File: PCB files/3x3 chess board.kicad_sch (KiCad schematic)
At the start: 81 parts, among them J1 Conn_01x03, J10 Conn_01x02, J11 USB4216-03-A_REVA, J12 Conn_01x03, J2 Conn_01x03, J4 Conn_01x03, J5 Conn_01x03, J6 Conn_01x03, J7 Conn_01x03, J8 Conn_01x03, J9 Conn_01x03, U1 MCP23S17_SO, U2 MCP23S17_SO, U3 W25Q128JVS, U4 RP2040, X1 ABM8-272-T3

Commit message: update
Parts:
- added D10: LED, symbol Device:LED
- added R25, R26, R27, R28: R, symbol Device:R
- added SW1, SW2: SW_DPST_x2, symbol Switch:SW_DPST_x2
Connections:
- net +3.3V: now also R25.1, R27.1, R28.1; no longer D1.2 (A), D2.2 (A), D3.2 (A), D4.2 (A), D5.2 (A), D6.2 (A), D7.2 (A), D8.2 (A), D9.2 (A), U1.18 (~{RESET}), U2.18 (~{RESET})
- net GND: now also D1.1 (K), D2.1 (K), D3.1 (K), D4.1 (K), D5.1 (K), D6.1 (K), D7.1 (K), D8.1 (K), D9.1 (K), D10.1 (K), SW1.1 (A), SW2.1 (A)
- net at R7.2: now also D5.2 (A); no longer D7.1 (K)
- net at R5.2: now also D7.2 (A); no longer D5.1 (K)
- net at R1.2: now also D2.2 (A); no longer D4.1 (K)
- net at R3.1: now also D4.2 (A); no longer D2.1 (K)
- net at R4.2: now also D3.2 (A); no longer D3.1 (K)
- net at R9.2: now also D9.2 (A); no longer D9.1 (K)
- net at R8.2: now also D8.2 (A); no longer D8.1 (K)
- net at R6.2: now also D6.2 (A); no longer D6.1 (K)
- net at R2.2: now also D1.2 (A); no longer D1.1 (K)
- new net: R28.2, SW1.2 (B), U1.18 (~{RESET})
- new net: R27.2, SW2.2 (B), U2.18 (~{RESET})
- new net: D10.2 (A), R25.2
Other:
- note added: "replace with esp 32 and esp prog"
- note added: "testing voltage regulator"
- moved on the sheet: D1, D2, D3, D4, D5, D6, D7, D8, D9, TP1, TP2, TP3

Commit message: update
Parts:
- removed C2: 0.1uF, Capacitor_SMD:C_0805_2012Metric, symbol Device:C
- removed C21, C22: 1uF, Capacitor_SMD:C_0805_2012Metric_Pad1.18x1.45mm_HandSolder, symbol Device:C
- removed J10: Conn_01x02, Connector_PinHeader_2.54mm:PinHeader_1x02_P2.54mm_Vertical, symbol Connector_Generic:Conn_01x02
- removed J11: USB4216-03-A_REVA, USB receptacle:USB 2.0, symbol USB C 2.0 receptacle:USB4216-03-A_REVA
- removed R27: R, symbol Device:R
- removed SW2: SW_DPST_x2, symbol Switch:SW_DPST_x2
- removed TP10, TP4, TP5, TP7, TP8: TestPoint, TestPoint:TestPoint_Pad_2.0x2.0mm, symbol Connector:TestPoint
- removed U2: MCP23S17_SO, Package_SO:SOIC-28W_7.5x17.9mm_P1.27mm, symbol Interface_Expansion:MCP23S17_SO
- removed U3: W25Q128JVS, Package_SO:SOIC-8_5.3x5.3mm_P1.27mm, symbol Memory_Flash:W25Q128JVS
- removed U4: RP2040, Package_DFN_QFN:QFN-56-1EP_7x7mm_P0.4mm_EP3.2x3.2mm, symbol MCU_RaspberryPi:RP2040
- removed X1: ABM8-272-T3, ABM8 - 272 - T3:ABM8-272-T3_ABR, symbol ABM8-272-T3:ABM8-272-T3
- added D11: LED, symbol Device:LED
- added D12, D13, D14, D15, D16, D17, D18: LED, Diode_SMD:D_0805_2012Metric_Pad1.15x1.40mm_HandSolder, symbol Device:LED
- added J10, J11, J13, J14, J15, J16, J17: Conn_01x03, Hall effect sensor:TSOT-3L_MLX92232LSE-AAA-002-SP_MEL, symbol Connector_Generic:Conn_01x03
- added J3: Conn_02x03_Odd_Even, symbol Connector_Generic:Conn_02x03_Odd_Even
- added R29: 5k, Resistor_SMD:R_0805_2012Metric_Pad1.20x1.40mm_HandSolder, symbol Device:R
- added R30: R, symbol Device:R
- added R31, R32, R33, R34, R35, R36, R37: 16, Resistor_SMD:R_0805_2012Metric_Pad1.20x1.40mm_HandSolder, symbol Device:R
- added U3: ESP32-S3-WROOM-1, RF_Module:ESP32-S3-WROOM-1, symbol RF_Module:ESP32-S3-WROOM-1
- C14, C15: value 15pF -> 10nF
- C16, C17, C18, C19, C20: value 0.1uF -> 10nF
- R10: value 1k -> R; footprint Resistor_SMD:R_0805_2012Metric_Pad1.20x1.40mm_HandSolder -> (none)
- R11: value do not fit -> R; footprint Resistor_SMD:R_0805_2012Metric_Pad1.20x1.40mm_HandSolder -> (none)
- R12: value 1k -> 5k
- R13, R14: value 27.4 -> 5k; footprint Resistor_SMD:R_1210_3225Metric_Pad1.30x2.65mm_HandSolder -> Resistor_SMD:R_0805_2012Metric_Pad1.20x1.40mm_HandSolder
- R15, R16: value 5.1kΩ -> 5k
- R26: value R -> 5k; footprint (none) -> Resistor_SMD:R_0805_2012Metric_Pad1.20x1.40mm_HandSolder
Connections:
- net +1V1 is gone; now on net GND: C17.1
- net D+ is gone; now on net HALL11: R13.1
- net D- is gone; now on net HALL12: R14.1
- net XIN is gone; now on net +3.3V: C14.2
- net XOUT is gone; now on net +3.3V: R12.2
- net +3.3V: now also C15.2, C16.2, C17.2, C18.2, C19.2, C20.2, R11.2, R13.2, R14.2, R15.2, R16.2, R26.2, J10.1 (Pin_1), J11.1 (Pin_1), J13.1 (Pin_1), J14.1 (Pin_1), J15.1 (Pin_1), J16.1 (Pin_1), J17.1 (Pin_1), J3.2 (Pin_2), R29.2, U3.2 (3V3); no longer C16.1, C18.1, C19.1, C20.1, R11.1
- net CS_{extender1}: now also U3.10 (IO17)
- net CS_{extender2}: now also U3.11 (IO18)
- net GND: now also C15.1, C16.1, C18.1, C19.1, C20.1, D11.1 (K), D12.1 (K), D13.1 (K), D14.1 (K), D15.1 (K), D16.1 (K), D17.1 (K), D18.1 (K), J10.2 (Pin_2), J11.2 (Pin_2), J13.2 (Pin_2), J14.2 (Pin_2), J15.2 (Pin_2), J16.2 (Pin_2), J17.2 (Pin_2), J3.4 (Pin_4), U3.1 (GND), U3.40 (GND), U3.41 (GND); no longer C15.2, C16.2, C17.2, C18.2, C19.2, C20.2, R15.2, R16.2
- net HALL1: now also U1.1 (GPB0), R34.2; no longer U1.25 (GPA4)
- net HALL2: now also U1.2 (GPB1), R33.2; no longer U1.27 (GPA6)
- net HALL3: now also R5.2, U1.3 (GPB2); no longer U1.22 (GPA1)
- net HALL4: now also R3.2, U1.4 (GPB3)
- net HALL5: now also U1.5 (GPB4), R35.2
- net HALL6: now also U1.6 (GPB5), R32.2
- net HALL7: now also R6.2, U1.7 (GPB6)
- net HALL8: now also R1.2, U1.8 (GPB7)
- net HALL9: now also U1.21 (GPA0), R36.2
- net INTA_{extender1}: now also U3.39 (IO1)
- net INTA_{extender2}: now also U3.15 (IO3)
- net INTB_{extender1}: now also U3.38 (IO2)
- net INTB_{extender2}: now also U3.4 (IO4)
- net MISO: now also U3.21 (IO13)
- net MOSI: now also U3.19 (IO11)
- net SCK: now also U3.20 (IO12)
- net at R7.1: now also D7.2 (A); no longer U1.26 (GPA5)
- net at D5.2 (A): now also R5.1; no longer R7.2
- net HALL14: now reaches R16.1
- net HALL14: now also R9.2, U1.26 (GPA5), J15.3 (Pin_3)
- net HALL10: now reaches R12.1
- net HALL10: now also U1.22 (GPA1), J10.3 (Pin_3), R31.2; no longer C15.1
- net at D3.2 (A): now also R4.1; no longer R4.2
- net HALL13: now reaches R15.1
- net HALL13: now also U1.25 (GPA4), J14.3 (Pin_3), R37.2
- net HALL11: now reaches U1.23 (GPA2)
- net HALL11: now also R7.2, J11.3 (Pin_3); no longer R5.1
- net at R6.1: now also D6.2 (A); no longer U1.24 (GPA3)
- net at R1.1: now also D1.2 (A); no longer U1.28 (GPA7)
- net at D2.2 (A): now also R2.1; no longer R1.2
- net at D9.2 (A): now also R9.1; no longer R9.2
- net at D8.2 (A): now also R8.1; no longer R8.2
- net HALL15: now reaches R26.1
- net HALL15: now also R8.2, U1.27 (GPA6), J16.3 (Pin_3)
- net HALL12: now reaches R2.2
- net HALL12: now also U1.24 (GPA3), J13.3 (Pin_3); no longer D1.2 (A)
- net CS_{flash}: no longer names the net of R10.2
- net CS_{flash}: no longer R11.2
- new net: D14.2 (A), R33.1
- new net: D18.2 (A), R37.1
- new net: D13.2 (A), R32.1
- new net: D12.2 (A), R31.1
- new net: D11.2 (A), R30.2
- new net: D15.2 (A), R34.1
- new net: D16.2 (A), R35.1
- new net: D17.2 (A), R36.1
- new net EN: J3.1 (Pin_1), R11.1, U3.3 (EN)
- new net HALL16: J17.3 (Pin_3), R29.1, R4.2, U1.28 (GPA7)
- new net IO0: J3.6 (Pin_6), U3.27 (IO0)
- new net LED_test: R30.1, U3.23 (IO21)
- new net RX: J3.5 (Pin_5), U3.36 (RXD0)
- new net TX: J3.3 (Pin_3), U3.37 (TXD0)
- no-connect marks 35 -> 5
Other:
- note added: "Hall effect sensor 10"
- note added: "Hall effect sensor 11"
- note added: "Hall effect sensor 12"
- note added: "Hall effect sensor 13"
- note added: "Hall effect sensor 14"
- note added: "Hall effect sensor 15"
- note added: "Hall effect sensor 16"
- note added: "testing MCU"
- note removed: "MLX92213"
- note removed: "RP2040 MCU"
- note removed: "connect pin 1 and 2 w/ jumper to pull CS low"
- note removed: "replace with esp 32 and esp prog"
- note removed: "we can technically have 8 extenders per one cs, but i think we just use mult cs"
- moved on the sheet: C1, C10, C11, C12, C13, C3, C4, C5, C6, C7, C8, C9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

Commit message: update schematic and and pcb w/ new mcu
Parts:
- removed C8: 10uF, Capacitor_SMD:C_0805_2012Metric, symbol Device:C
- removed D17, D18: LED, Diode_SMD:D_0805_2012Metric_Pad1.15x1.40mm_HandSolder, symbol Device:LED
- removed LMS1585: ~, LMS1585:KTT0003B, symbol LM5158:LMS1585
- removed R1, R31, R32, R33, R34, R35, R36, R37, R6: 16, Resistor_SMD:R_0805_2012Metric_Pad1.20x1.40mm_HandSolder, symbol Device:R
- removed R25: R, symbol Device:R
- removed SW1: SW_DPST_x2, symbol Switch:SW_DPST_x2
- removed TP1, TP3, TP6: TestPoint, TestPoint:TestPoint_Pad_2.0x2.0mm, symbol Connector:TestPoint
- removed TP2: Ground test point, TestPoint:TestPoint_Pad_2.0x2.0mm, symbol Connector:TestPoint
- added C2, C22: 0.1uF, Capacitor_SMD:C_0805_2012Metric, symbol Device:C
- added C21, C4: 1uF, Capacitor_SMD:C_0805_2012Metric, symbol Device:C
- added D11: LED, Diode_SMD:D_0805_2012Metric_Pad1.15x1.40mm_HandSolder, symbol Device:LED
- added R11, R12, R13, R14, R15, R16, R17, R18, R3: 16, Resistor_SMD:R_0805_2012Metric_Pad1.20x1.40mm_HandSolder, symbol Device:R
- added U2: MCP23S17_SO, Package_SO:SOIC-28W_7.5x17.9mm_P1.27mm, symbol Interface_Expansion:MCP23S17_SO
- C3: value 10uF -> 1uF
- D10: footprint (none) -> Diode_SMD:D_0805_2012Metric_Pad1.15x1.40mm_HandSolder
- D17: renamed from D11; footprint (none) -> Diode_SMD:D_0805_2012Metric_Pad1.15x1.40mm_HandSolder
- J17: renamed from J3; footprint (none) -> Connector_IDC:IDC-Header_2x03_P2.54mm_Vertical
- R1: renamed from R28; value R -> 5k; footprint (none) -> Resistor_SMD:R_0805_2012Metric_Pad1.20x1.40mm_HandSolder
- R10: value R -> 16; footprint (none) -> Resistor_SMD:R_0805_2012Metric_Pad1.20x1.40mm_HandSolder
- R2: value 16 -> 5k
- R30: value R -> 320; footprint (none) -> Resistor_SMD:R_0805_2012Metric_Pad1.20x1.40mm_HandSolder
- R35: renamed from R11; value R -> 5k; footprint (none) -> Resistor_SMD:R_0805_2012Metric_Pad1.20x1.40mm_HandSolder
- renumbered C5 to C10, C4 to C11, C13 to C12, C15 to C13, C16 to C14, C14 to C15, C7 to C16, C19 to C17, C20 to C18, C17 to C19, C18 to C20, C12 to C5, C9 to C6, C10 to C7, C11 to C8, C6 to C9, J5 to J1, J13 to J10, J10 to J11, J2 to J12, J16 to J13, J17 to J14, J14 to J15, J15 to J16, J7 to J2, J6 to J3, J12 to J4, J9 to J5, J1 to J6, J4 to J7, J11 to J9, R18 to R19, R22 to R20, R17 to R21, R19 to R22, R20 to R23, R21 to R24, R23 to R25, R13 to R26, R14 to R27, R12 to R28, R24 to R29, R26 to R31, R29 to R32, R15 to R33, R16 to R34, R3 to R6
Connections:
- net VBUS is gone; now on net GND: C3.1
- net +3.3V: now also C3.2, R2.1, C2.2, C21.2, C22.2, C4.2, U2.9 (VDD)
- net CS_{extender1}: now also U3.24 (IO47); no longer U1.11 (~{CS}), U3.10 (IO17)
- net CS_{extender2}: now also U3.25 (IO48), U2.11 (~{CS}); no longer U3.11 (IO18)
- net GND: now also C2.1, C21.1, C22.1, C4.1, D11.1 (K), U2.10 (VSS), U2.15 (A0), U2.16 (A1), U2.17 (A2); no longer C3.2
- net HALL10: now also U2.2 (GPB1); no longer U1.22 (GPA1)
- net HALL11: now also U2.3 (GPB2); no longer R7.2, U1.23 (GPA2)
- net HALL12: now also U2.4 (GPB3); no longer R2.2, U1.24 (GPA3)
- net HALL13: now also U2.5 (GPB4); no longer U1.25 (GPA4)
- net HALL14: now also U2.6 (GPB5); no longer R9.2, U1.26 (GPA5)
- net HALL15: now also U2.7 (GPB6); no longer R8.2, U1.27 (GPA6)
- net HALL16: now also U2.8 (GPB7); no longer R4.2, U1.28 (GPA7)
- net HALL3: no longer R5.2
- net HALL4: no longer R6.2
- net HALL9: now also U2.1 (GPB0); no longer U1.21 (GPA0)
- net INTA_{extender1}: now also U3.17 (IO9); no longer U3.39 (IO1)
- net INTA_{extender2}: now also U2.20 (INTA)
- net INTB_{extender1}: now also U3.18 (IO10); no longer U3.38 (IO2)
- net INTB_{extender2}: now also U3.16 (IO46), U2.19 (INTB); no longer U3.4 (IO4)
- net LED_test: now also U3.5 (IO5); no longer U3.23 (IO21)
- net MISO: now also U2.14 (SO)
- net MOSI: now also U2.13 (SI)
- net SCK: now also U2.12 (SCK)
- net at D14.2 (A): now also R16.2
- net at D3.2 (A): now also R5.2; no longer R4.1
- net at D6.2 (A): now also R8.2
- net at D2.2 (A): now also R4.2; no longer R2.1
- net at R7.1: now also U1.25 (GPA4); no longer D7.2 (A)
- net at R8.1: now also U1.26 (GPA5); no longer D8.2 (A)
- net at D13.2 (A): now also R15.2
- net at D12.2 (A): now also R14.2
- net at D15.2 (A): now also R17.2
- net at D1.2 (A): now also R3.2
- net at D16.2 (A): now also R18.2
- net at R9.1: now also U1.27 (GPA6); no longer D9.2 (A)
- net at R10.1: now also U1.28 (GPA7)
- net at R10.2: now also D8.2 (A)
- net at D10.2 (A): now also R12.2
- net at D5.2 (A): now also R7.2; no longer R5.1
- new net: R17.1, U2.27 (GPA6)
- new net: R6.2, U1.24 (GPA3)
- new net: D11.2 (A), R13.2
- new net: D7.2 (A), R9.2
- new net: R3.1, U1.21 (GPA0)
- new net: R4.1, U1.22 (GPA1)
- new net: R5.1, U1.23 (GPA2)
- new net: R16.1, U2.26 (GPA5)
- new net: R2.2, U2.18 (~{RESET})
- new net: D9.2 (A), R11.2
- new net: R15.1, U2.25 (GPA4)
- new net: R12.1, U2.22 (GPA1)
- new net: R13.1, U2.23 (GPA2)
- new net: R14.1, U2.24 (GPA3)
- new net: R18.1, U2.28 (GPA7)
- new net: R11.1, U2.21 (GPA0)
- no-connect marks 5 -> 23
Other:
- note added: "esp PROG"
- note removed: "3.3 voltage regulator"
- note removed: "active low resets internally"
- note removed: "testing voltage regulator"
- moved on the sheet: C1, C10, C11, C12, C13, C14, C15, C16, C17, C18, C19, C20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

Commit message: changes
added promotion buttons, removed interrupts, cleaned up silkscreen
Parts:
- added R36: 5k, Resistor_SMD:R_0805_2012Metric_Pad1.20x1.40mm_HandSolder, symbol Device:R
- added R37, R38, R39, R40: 10k, Resistor_SMD:R_0805_2012Metric_Pad1.20x1.40mm_HandSolder, symbol Device:R
- added SW1, SW2, SW3, SW4: SW_Push, Button_Switch_THT:SW_PUSH_6mm_H4.3mm, symbol Switch:SW_Push
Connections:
- net +3.3V: now also R36.2, R37.2, R38.2, R39.2, R40.2
- net IO0: now also R36.1
- net Bishop_promote: now reaches U3.10 (IO17)
- net Bishop_promote: now also SW1.1
- net Rook_promote: now reaches U3.11 (IO18)
- net Rook_promote: now also SW2.1
- net Queen_promote: now reaches U3.12 (IO8)
- net Queen_promote: now also SW4.1
- net Knight_promote: now reaches U3.9 (IO16)
- net Knight_promote: now also SW3.1
- net INTA_{extender1}: no longer names the net of U3.17 (IO9)
- net INTA_{extender1}: no longer U1.20 (INTA)
- net INTA_{extender2}: no longer names the net of U3.15 (IO3)
- net INTA_{extender2}: no longer U2.20 (INTA)
- net INTB_{extender1}: no longer names the net of U3.18 (IO10)
- net INTB_{extender1}: no longer U1.19 (INTB)
- net INTB_{extender2}: no longer names the net of U3.16 (IO46)
- net INTB_{extender2}: no longer U2.19 (INTB)
- new net: R40.1, SW3.2
- new net: R39.1, SW1.2
- new net: R38.1, SW4.2
- new net: R37.1, SW2.2
- no-connect marks 23 -> 27
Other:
- moved on the sheet: C21, C22, J17, R35, U3

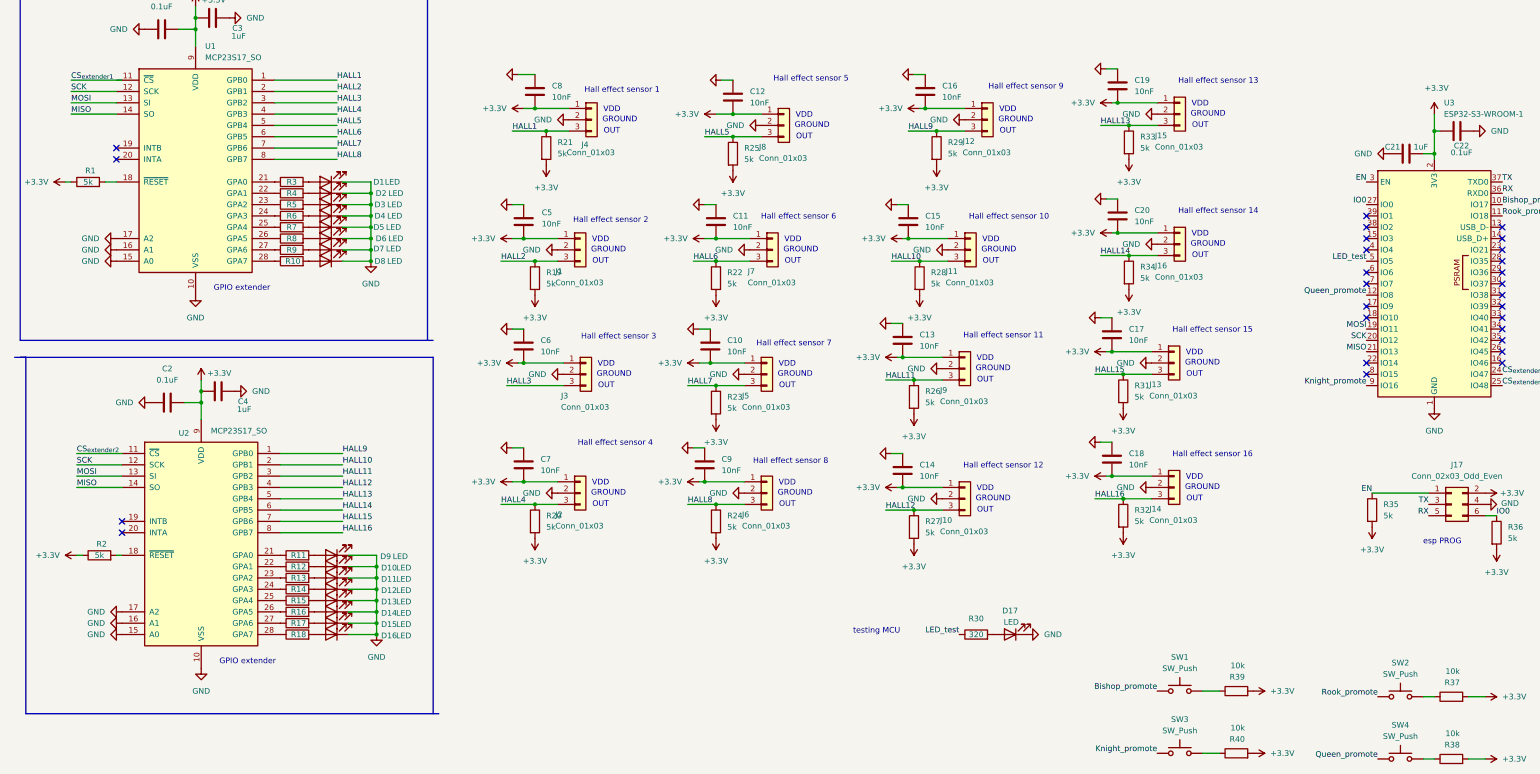
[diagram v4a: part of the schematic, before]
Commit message: adjustments before ordering
udpated res values, added gerber files and parts list files
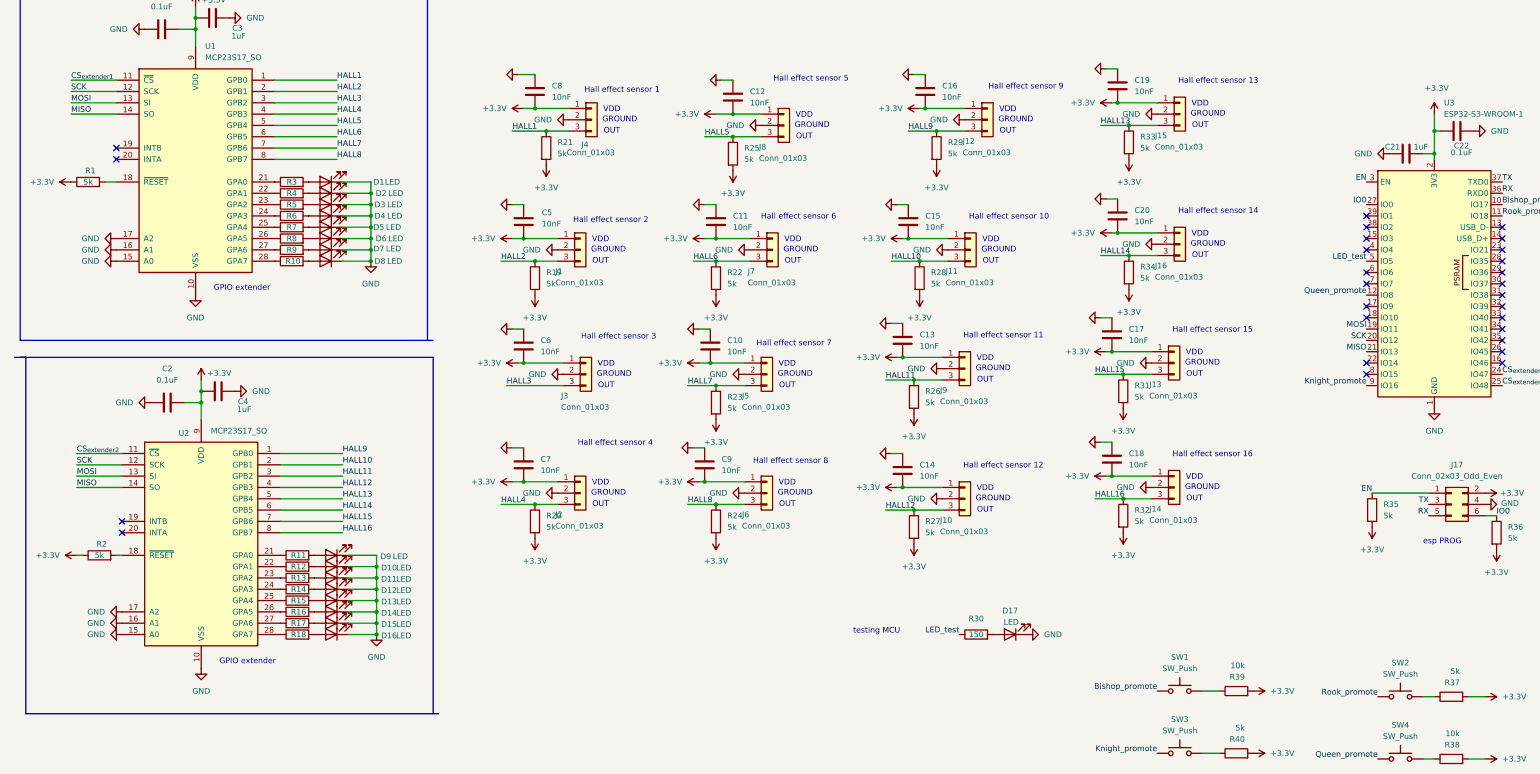
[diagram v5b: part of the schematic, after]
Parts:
- R10, R11, R12, R13, R14, R15, R16, R17, R18, R3, R4, R5, R6, R7, R8, R9: value 16 -> 150
- R30: value 320 -> 150
- R37, R40: value 10k -> 5k
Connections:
- net CS_{extender1}: now also U1.11 (~{CS})
